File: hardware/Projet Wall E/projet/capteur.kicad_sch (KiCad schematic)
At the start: 11 parts, among them J6 Conn_01x06, J7 Conn_01x06, J8 Conn_01x06

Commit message: feat: mise a jour reference jlcpcb
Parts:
- C25, C27, C29: footprint Capacitor_SMD:C_0603_1608Metric -> Capacitor_SMD:C_0402_1005Metric; JLCPCB Part (none) -> C1525
- C26, C28, C30: footprint Capacitor_SMD:C_0603_1608Metric -> Capacitor_SMD:C_0402_1005Metric; JLCPCB Part (none) -> C15525
- J6, J7, J8: footprint Connector_JST:JST_PH_B6B-PH-K_1x06_P2.00mm_Vertical -> Connector_PinHeader_2.54mm:PinHeader_1x06_P2.54mm_Vertical
- R18, R19: footprint Resistor_SMD:R_0603_1608Metric -> Resistor_SMD:R_0402_1005Metric; JLCPCB Part (none) -> C850286; now not fitted
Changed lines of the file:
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@@
 			)
 		)
-		(property "Footprint" "Capacitor_SMD:C_0603_1608Metric"
+		(property "Footprint" "Capacitor_SMD:C_0402_1005Metric"
 			(at 43.18 100.33 0)
 			(hide yes)
@@
 		(property "Description" ""
 			(at 43.18 100.33 0)
+			(show_name no)
+			(do_not_autoplace no)
+			(effects
+				(font
+					(size 1.27 1.27)
+				)
+			)
+		)
+		(property "JLCPCB Part" "C15525"
+			(at 43.18 100.33 0)
+			(hide yes)
 			(show_name no)
 			(do_not_autoplace no)
@@
 			)
 		)
-		(property "Footprint" "Capacitor_SMD:C_0603_1608Metric"
+		(property "Footprint" "Capacitor_SMD:C_0402_1005Metric"
 			(at 106.68 97.79 0)
 			(hide yes)
@@
 		(property "Description" ""
 			(at 106.68 97.79 0)
+			(show_name no)
+			(do_not_autoplace no)
+			(effects
+				(font
+					(size 1.27 1.27)
+				)
+			)
+		)
+		(property "JLCPCB Part" "C1525"
+			(at 106.68 97.79 0)
+			(hide yes)
 			(show_name no)
 			(do_not_autoplace no)
@@
 			)
 		)
-		(property "Footprint" "Connector_JST:JST_PH_B6B-PH-K_1x06_P2.00mm_Vertical"
+		(property "Footprint" "Connector_PinHeader_2.54mm:PinHeader_1x06_P2.54mm_Vertical"
 			(at 219.71 87.63 0)
 			(hide yes)
@@
 			)
 		)
-		(property "Footprint" "Capacitor_SMD:C_0603_1608Metric"
+		(property "Footprint" "Capacitor_SMD:C_0402_1005Metric"
 			(at 30.48 100.33 0)
 			(hide yes)
@@
 		(property "Description" ""
 			(at 30.48 100.33 0)
+			(show_name no)
+			(do_not_autoplace no)
+			(effects
+				(font
+					(size 1.27 1.27)
+				)
+			)
+		)
+		(property "JLCPCB Part" "C1525"
+			(at 30.48 100.33 0)
+			(hide yes)
 			(show_name no)
 			(do_not_autoplace no)
@@
 			)
 		)
-		(property "Footprint" "Capacitor_SMD:C_0603_1608Metric"
+		(property "Footprint" "Capacitor_SMD:C_0402_1005Metric"
 			(at 119.38 97.79 0)
 			(hide yes)
@@
 		(property "Description" ""
 			(at 119.38 97.79 0)
+			(show_name no)
+			(do_not_autoplace no)
+			(effects
+				(font
+					(size 1.27 1.27)
+				)
+			)
+		)
+		(property "JLCPCB Part" "C15525"
+			(at 119.38 97.79 0)
+			(hide yes)
 			(show_name no)
 			(do_not_autoplace no)
@@
 		(on_board yes)
 		(in_pos_files yes)
-		(dnp no)
+		(dnp yes)
 		(property "Reference" "R18"
 			(at 243.84 88.9 0)
@@
 			)
 		)
-		(property "Footprint" "Resistor_SMD:R_0603_1608Metric"
+		(property "Footprint" "Resistor_SMD:R_0402_1005Metric"
 			(at 241.3 90.17 0)
 			(hide yes)
@@
 		(property "Description" ""
 			(at 241.3 90.17 0)
+			(show_name no)
+			(do_not_autoplace no)
+			(effects
+				(font
+					(size 1.27 1.27)
+				)
+			)
+		)
+		(property "JLCPCB Part" "C850286"
+			(at 241.3 90.17 0)
+			(hide yes)
 			(show_name no)
 			(do_not_autoplace no)
@@
 			)
 		)
-		(property "Footprint" "Capacitor_SMD:C_0603_1608Metric"
+		(property "Footprint" "Capacitor_SMD:C_0402_1005Metric"
 			(at 180.34 100.33 0)
 			(hide yes)
@@
 		(property "Description" ""
 			(at 180.34 100.33 0)
+			(show_name no)
+			(do_not_autoplace no)
+			(effects
+				(font
+					(size 1.27 1.27)
+				)
+			)
+		)
+		(property "JLCPCB Part" "C1525"
+			(at 180.34 100.33 0)
+			(hide yes)
 			(show_name no)
 			(do_not_autoplace no)
@@
 			)
 		)
-		(property "Footprint" "Capacitor_SMD:C_0603_1608Metric"
+		(property "Footprint" "Capacitor_SMD:C_0402_1005Metric"
 			(at 193.04 100.33 0)
 			(hide yes)
@@
 		(property "Description" ""
 			(at 193.04 100.33 0)
+			(show_name no)
+			(do_not_autoplace no)
+			(effects
+				(font
+					(size 1.27 1.27)
+				)
+			)
+		)
+		(property "JLCPCB Part" "C15525"
+			(at 193.04 100.33 0)
+			(hide yes)
 			(show_name no)
 			(do_not_autoplace no)
@@
 			)
 		)
-		(property "Footprint" "Connector_JST:JST_PH_B6B-PH-K_1x06_P2.00mm_Vertical"
+		(property "Footprint" "Connector_PinHeader_2.54mm:PinHeader_1x06_P2.54mm_Vertical"
 			(at 76.2 90.17 0)
 			(hide yes)
@@
 			)
 		)
-		(property "Footprint" "Connector_JST:JST_PH_B6B-PH-K_1x06_P2.00mm_Vertical"
+		(property "Footprint" "Connector_PinHeader_2.54mm:PinHeader_1x06_P2.54mm_Vertical"
 			(at 156.21 88.9 0)
 			(hide yes)
@@
 		(on_board yes)
 		(in_pos_files yes)
-		(dnp no)
+		(dnp yes)
 		(property "Reference" "R19"
 			(at 262.89 88.9 0)
@@
 			)
 		)
-		(property "Footprint" "Resistor_SMD:R_0603_1608Metric"
+		(property "Footprint" "Resistor_SMD:R_0402_1005Metric"
 			(at 260.35 90.17 0)
 			(hide yes)
@@
 			(show_name no)
 			(do_not_autoplace no)
+			(effects
+				(font
+					(size 1.27 1.27)
+				)
+			)
+		)
+		(property "JLCPCB Part" "C850286"
+			(at 260.35 90.17 0)
+			(hide yes)
+			(show_name no)
+			(do_not_autoplace no)

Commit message: Annotation par feuille + références JLCPCB Part #
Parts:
- C501: renamed from C25; JLCPCB Part C1525 -> (none); JLCPCB Part# (none) -> C1525
- C502: renamed from C26; JLCPCB Part C15525 -> (none); JLCPCB Part# (none) -> C15525
- C503: renamed from C27; JLCPCB Part C1525 -> (none); JLCPCB Part# (none) -> C1525
- C504: renamed from C28; JLCPCB Part C15525 -> (none); JLCPCB Part# (none) -> C15525
- C505: renamed from C29; JLCPCB Part C1525 -> (none); JLCPCB Part# (none) -> C1525
- C506: renamed from C30; JLCPCB Part C15525 -> (none); JLCPCB Part# (none) -> C15525
- J501: renamed from J6; JLCPCB Part# (none) -> C37208
- J502: renamed from J7; JLCPCB Part# (none) -> C37208
- J503: renamed from J8; JLCPCB Part# (none) -> C37208
- R501: renamed from R18; JLCPCB Part C850286 -> (none); JLCPCB Part# (none) -> C850286
- R502: renamed from R19; JLCPCB Part C850286 -> (none); JLCPCB Part# (none) -> C850286

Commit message: Intégration feuille capteurs + MCU/software en cours
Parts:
- added C507, C508, C509: 100n, Capacitor_SMD:C_0402_1005Metric, symbol Device:C_Small
- added D5: WS2812B, LED_SMD:LED_WS2812B-Mini_PLCC4_3.5x3.5mm, symbol LED:WS2812B
- added J1: Conn_01x03, Connector_Audio:Jack_XLR_Neutrik_NC3FAAH_Horizontal, symbol Connector_Generic:Conn_01x03
- added U6: SN74AHCT1G125DBVR, Package_TO_SOT_SMD:SOT-23-5, symbol 74xGxx:74AHCT1G125
- C25: renamed from C501; JLCPCB Part (none) -> C1525; JLCPCB Part# C1525 -> (none)
- C26: renamed from C502; JLCPCB Part (none) -> C15525; JLCPCB Part# C15525 -> (none)
- C27: renamed from C503; JLCPCB Part (none) -> C1525; JLCPCB Part# C1525 -> (none)
- C28: renamed from C504; JLCPCB Part (none) -> C15525; JLCPCB Part# C15525 -> (none)
- C29: renamed from C505; JLCPCB Part (none) -> C1525; JLCPCB Part# C1525 -> (none)
- C30: renamed from C506; JLCPCB Part (none) -> C15525; JLCPCB Part# C15525 -> (none)
- J6: renamed from J501; JLCPCB Part# C37208 -> (none)
- J7: renamed from J502; JLCPCB Part# C37208 -> (none)
- J8: renamed from J503; JLCPCB Part# C37208 -> (none)
- R18: renamed from R501; JLCPCB Part (none) -> C850286; JLCPCB Part# C850286 -> (none)
- R19: renamed from R502; JLCPCB Part (none) -> C850286; JLCPCB Part# C850286 -> (none)
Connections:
- net GND: now also C507.2, C508.1, C509.2, D5.3 (VSS), J1.3 (Pin_3), U6.1, U6.3 (GND)
- new net NEOPIXEL: U6.2
- new net NP_5V: D5.4 (DIN), J1.2 (Pin_2), U6.4
- new net VBUS: C507.1, C508.2, C509.1, D5.1 (VDD), J1.1 (Pin_1), U6.5 (VCC)
- no-connect marks 1 -> 2
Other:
- note added: "NEOPIXEL RGB LED"

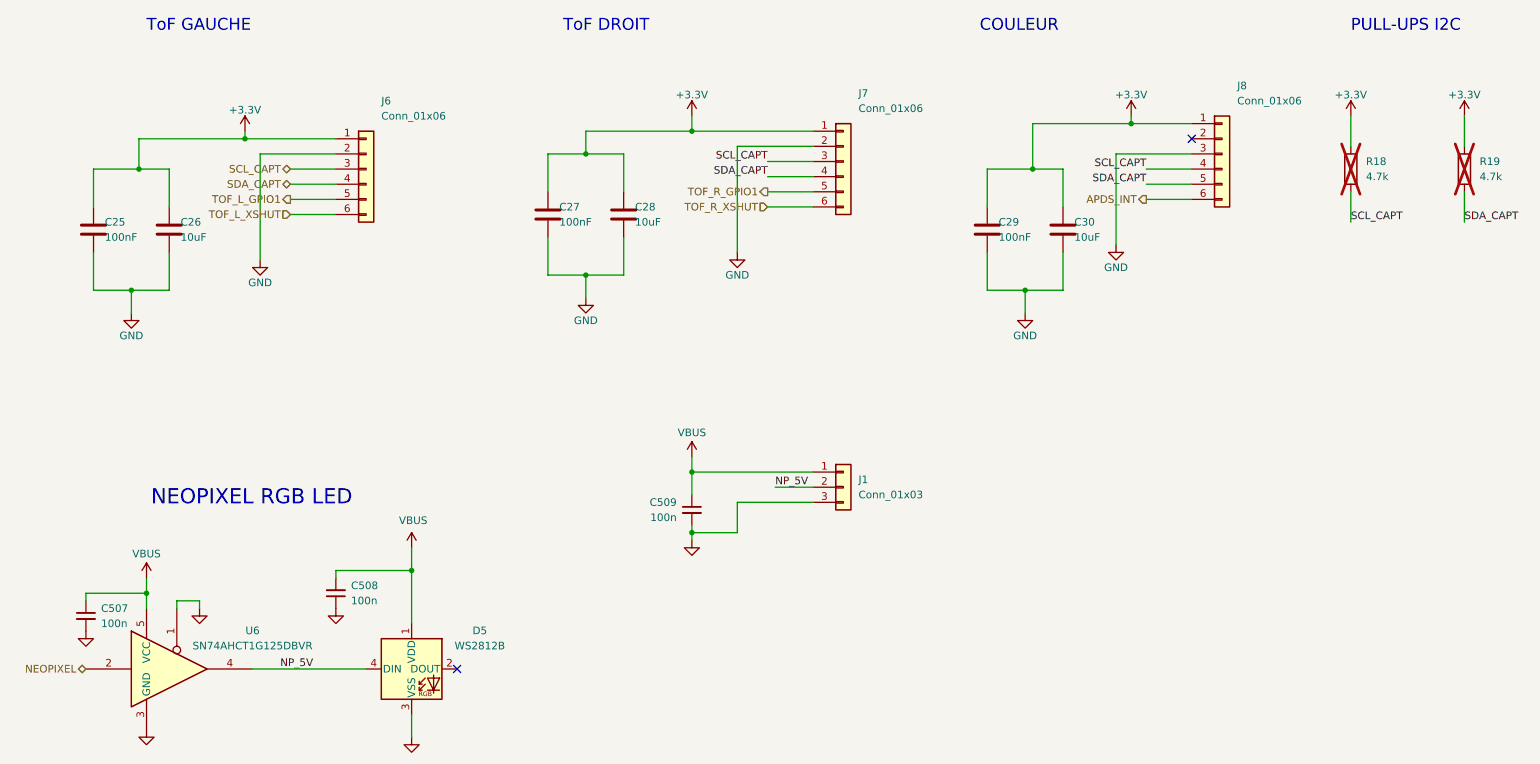
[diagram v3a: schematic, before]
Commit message: Schéma : 0 erreur ERC, pinout MCU finalisé + config .ioc
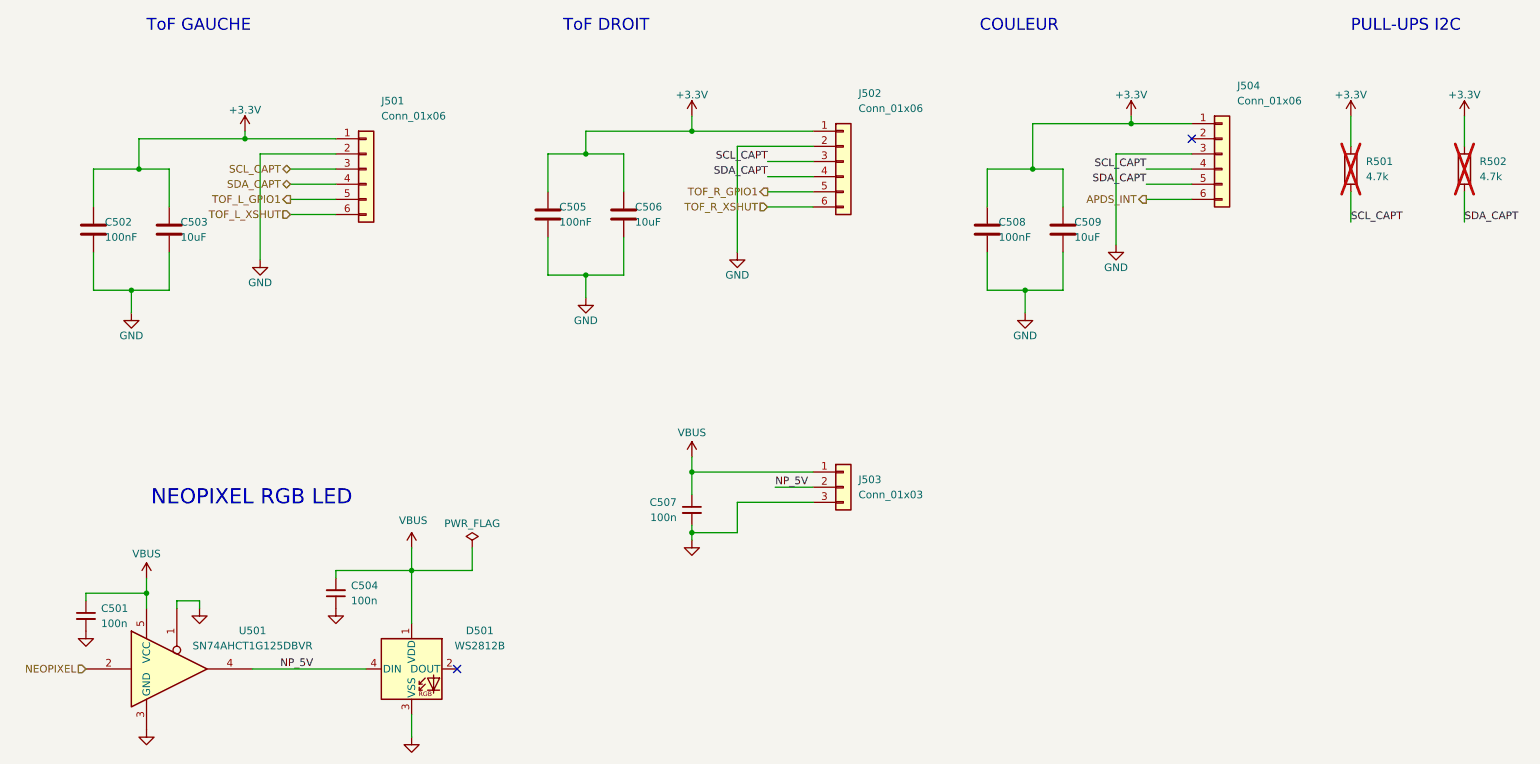
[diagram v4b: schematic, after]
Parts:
- renumbered C507 to C501, C25 to C502, C26 to C503, C508 to C504, C27 to C505, C28 to C506, C509 to C507, C29 to C508, C30 to C509, D5 to D501, J6 to J501, J7 to J502, J1 to J503, J8 to J504, R18 to R501, R19 to R502, U6 to U501

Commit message: Correction empreintes et références JLCPCB
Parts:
- C501, C504, C507: JLCPCB Part # C1525 -> (none); JLCPCB Part# (none) -> C1525
- C502, C505, C508: JLCPCB Part C1525 -> (none); JLCPCB Part# (none) -> C1525
- C503, C506, C509: JLCPCB Part C15525 -> (none); JLCPCB Part# (none) -> C15525
- D501: JLCPCB Part # C527089 -> (none); JLCPCB Part# (none) -> C527089
- J501, J502, J504: JLCPCB Part# (none) -> C37208
- J503: footprint Connector_Audio:Jack_XLR_Neutrik_NC3FAAH_Horizontal -> Connector_PinHeader_2.54mm:PinHeader_1x03_P2.54mm_Vertical
- R501, R502: JLCPCB Part C850286 -> (none); JLCPCB Part# (none) -> C850286
- U501: JLCPCB Part # C20617903 -> (none); JLCPCB Part# (none) -> C20617903

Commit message: verification finale effectue
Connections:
- net NP_5V: no longer J503.2 (Pin_2)
- net at D501.2 (DOUT): now also J503.2 (Pin_2)
- no-connect marks 2 -> 1
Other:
- moved on the sheet: C507, J503
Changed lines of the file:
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@@
 	)
 	(junction
-		(at 130.81 140.97)
+		(at 186.69 110.49)
 		(diameter 0)
 		(color 0 0 0 0)
 	)
 	(junction
-		(at 186.69 110.49)
+		(at 113.03 171.45)
 		(diameter 0)
 		(color 0 0 0 0)
@@
 	)
 	(junction
-		(at 130.81 151.13)
+		(at 113.03 181.61)
 		(diameter 0)
 		(color 0 0 0 0)
@@
 		(at 214.63 85.09)
 	)
-	(no_connect
-		(at 91.44 173.99)
-	)
 	(wire
 		(pts
@@
 	(wire
 		(pts
+			(xy 91.44 173.99) (xy 124.46 173.99)
+		)
+		(stroke
+			(width 0)
+			(type default)
+		)
+	)
+	(wire
+		(pts
 			(xy 83.82 157.48) (xy 83.82 166.37)
 		)
@@
 	(wire
 		(pts
-			(xy 130.81 140.97) (xy 151.13 140.97)
+			(xy 113.03 171.45) (xy 124.46 171.45)
 		)
 		(stroke
@@
 	(wire
 		(pts
-			(xy 130.81 140.97) (xy 130.81 144.78)
+			(xy 113.03 171.45) (xy 113.03 175.26)
 		)
 		(stroke
@@
 	(wire
 		(pts
-			(xy 130.81 151.13) (xy 130.81 152.4)
+			(xy 113.03 181.61) (xy 113.03 182.88)
 		)
 		(stroke
@@
 	(wire
 		(pts
-			(xy 130.81 151.13) (xy 138.43 151.13)
+			(xy 113.03 181.61) (xy 120.65 181.61)
 		)
 		(stroke
@@
 	(wire
 		(pts
-			(xy 138.43 146.05) (xy 138.43 151.13)
+			(xy 120.65 176.53) (xy 120.65 181.61)
 		)
 		(stroke
@@
 	(wire
 		(pts
-			(xy 130.81 138.43) (xy 130.81 140.97)
+			(xy 113.03 168.91) (xy 113.03 171.45)
 		)
 		(stroke
@@
 	(wire
 		(pts
-			(xy 151.13 146.05) (xy 138.43 146.05)
+			(xy 124.46 176.53) (xy 120.65 176.53)
 		)
 		(stroke
@@
 	(wire
 		(pts
-			(xy 144.78 143.51) (xy 151.13 143.51)
-		)
-		(stroke
-			(width 0)
-			(type default)
-		)
-	)
-	(wire
-		(pts
 			(xy 83.82 157.48) (xy 71.12 157.48)
 		)
@@
 	(wire
 		(pts
-			(xy 130.81 149.86) (xy 130.81 151.13)
+			(xy 113.03 180.34) (xy 113.03 181.61)
 		)
 		(stroke
@@
 		)
 	)
-	(label "NP_5V"
-		(at 144.78 143.51 0)
-		(effects
-			(font
-				(size 1.27 1.27)
-			)
-			(justify left bottom)
-		)
-	)
 	(label "SDA_CAPT"
 		(at 207.01 92.71 180)
@@
 	(symbol
 		(lib_id "Connector_Generic:Conn_01x03")
-		(at 156.21 143.51 0)
+		(at 129.54 173.99 0)
 		(unit 1)
 		(body_style 1)
@@
 		(fields_autoplaced yes)
 		(property "Reference" "J503"
-			(at 158.75 142.2399 0)
+			(at 132.08 172.7199 0)
 			(show_name no)
 			(do_not_autoplace no)
@@
 		)
 		(property "Value" "Conn_01x03"
-			(at 158.75 144.7799 0)
+			(at 132.08 175.2599 0)
 			(show_name no)
 			(do_not_autoplace no)
@@
 		)
 		(property "Footprint" "Connector_PinHeader_2.54mm:PinHeader_1x03_P2.54mm_Vertical"
-			(at 156.21 143.51 0)
+			(at 129.54 173.99 0)
 			(hide yes)
 			(show_name no)
@@
 		)
 		(property "Datasheet" ""
-			(at 156.21 143.51 0)
+			(at 129.54 173.99 0)
 			(hide yes)
 			(show_name no)
@@
 		)
 		(property "Description" "Generic connector, single row, 01x03, script generated (kicad-library-utils/schlib/autogen/connector/)"
-			(at 156.21 143.51 0)
+			(at 129.54 173.99 0)
 			(hide yes)
 			(show_name no)
@@
 		)
 		(property "JLCPCB Part#" "C49257"
-			(at 156.21 143.51 0)
+			(at 129.54 173.99 0)
 			(hide yes)
 			(show_name no)
@@
 		)
 		(property "KLC_S3.3" ""
-			(at 156.21 143.51 0)
+			(at 129.54 173.99 0)
 			(hide yes)
 			(show_name no)
@@
 		)
 		(property "KLC_S4.1" ""
-			(at 156.21 143.51 0)
+			(at 129.54 173.99 0)
 			(hide yes)
 			(show_name no)
@@
 		)
 		(property "Sim.Device" ""
-			(at 156.21 143.51 0)
+			(at 129.54 173.99 0)
 			(hide yes)
 			(show_name no)
@@
 	(symbol
 		(lib_id "power:+5V")
-		(at 130.81 138.43 0)
+		(at 113.03 168.91 0)
 		(unit 1)
 		(body_style 1)
@@
 		(dnp no)
 		(property "Reference" "#PWR0513"
-			(at 130.81 142.24 0)
+			(at 113.03 172.72 0)
 			(hide yes)
 			(show_name no)
@@
 		)
 		(property "Value" "VBUS"
-			(at 130.81 134.366 0)
+			(at 113.03 164.846 0)
 			(show_name no)
 			(do_not_autoplace no)
@@
 		)
 		(property "Footprint" ""
-			(at 130.81 138.43 0)
+			(at 113.03 168.91 0)
 			(hide yes)
 			(show_name no)
@@
 		)
 		(property "Datasheet" ""
-			(at 130.81 138.43 0)
+			(at 113.03 168.91 0)
 			(hide yes)
 			(show_name no)
@@
 		)
 		(property "Description" "Power symbol creates a global label with name \"+5V\""
-			(at 130.81 138.43 0)
+			(at 113.03 168.91 0)
 			(hide yes)
 			(show_name no)
@@
 	(symbol
 		(lib_id "power:GND")
-		(at 130.81 152.4 0)
+		(at 113.03 182.88 0)
 		(unit 1)
 		(body_style 1)
@@
 		(fields_autoplaced yes)
 		(property "Reference" "#PWR0514"
-			(at 130.81 158.75 0)
+			(at 113.03 189.23 0)
 			(hide yes)
 			(show_name no)
@@
 		)
 		(property "Value" "GND"
-			(at 130.81 157.48 0)
+			(at 113.03 187.96 0)
 			(hide yes)
 			(show_name no)
@@
 		)
 		(property "Footprint" ""
-			(at 130.81 152.4 0)
+			(at 113.03 182.88 0)
 			(hide yes)
 			(show_name no)
@@
 		)
 		(property "Datasheet" ""
-			(at 130.81 152.4 0)
+			(at 113.03 182.88 0)
 			(hide yes)
 			(show_name no)
@@
 		)
 		(property "Description" "Power symbol creates a global label with name \"GND\" , ground"
-			(at 130.81 152.4 0)
+			(at 113.03 182.88 0)
 			(hide yes)
 			(show_name no)
@@
 	(symbol
 		(lib_id "Device:C_Small")
-		(at 130.81 147.32 0)
+		(at 113.03 177.8 0)
 		(mirror y)
 		(unit 1)
@@
 		(dnp no)
 		(property "Reference" "C507"
-			(at 128.27 146.0562 0)
+			(at 110.49 176.5362 0)
 			(show_name no)
 			(do_not_autoplace no)
@@
 		)
 		(property "Value" "100n"
-			(at 128.27 148.5962 0)
+			(at 110.49 179.0762 0)
 			(show_name no)
 			(do_not_autoplace no)
@@
 		)
 		(property "Footprint" "Capacitor_SMD:C_0402_1005Metric"
-			(at 130.81 147.32 0)
+			(at 113.03 177.8 0)
 			(hide yes)
 			(show_name no)
@@
 		)
 		(property "Datasheet" ""
-			(at 130.81 147.32 0)
+			(at 113.03 177.8 0)
 			(hide yes)
 			(show_name no)
@@
 		)
 		(property "Description" "Unpolarized capacitor, small symbol"
-			(at 130.81 147.32 0)
+			(at 113.03 177.8 0)
 			(hide yes)
 			(show_name no)
@@
 		)
 		(property "JLCPCB Part #" ""
-			(at 130.81 147.32 0)
+			(at 113.03 177.8 0)
 			(hide yes)
 			(show_name no)
@@
 		)
 		(property "JLCPCB Part#" "C1525"
-			(at 130.81 147.32 0)
+			(at 113.03 177.8 0)
 			(hide yes)
 			(show_name no)
@@
 		)
 		(property "Sim.Device" ""
-			(at 130.81 147.32 0)
+			(at 113.03 177.8 0)
 			(hide yes)
 			(show_name no)
